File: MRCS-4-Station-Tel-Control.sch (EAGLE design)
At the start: 19 parts, among them CON1 LEDs and Buttons RJ, CON2 LEDS & Pwr RJ, J1 LEDs & Buttons ST, J2 LEDS & Pwr ST

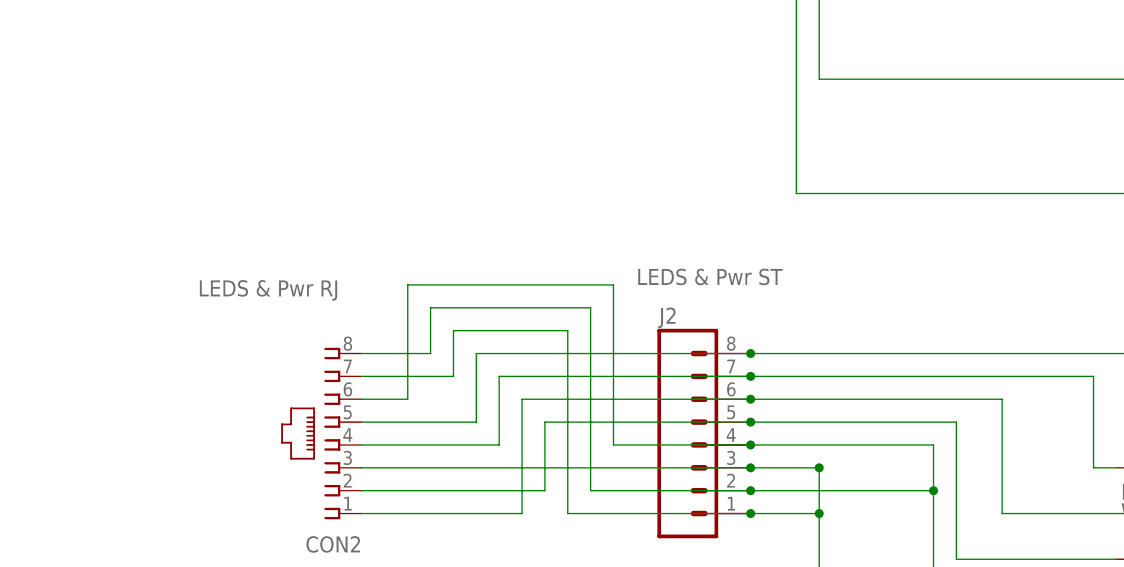
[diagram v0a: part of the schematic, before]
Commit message: Moved labels for push buttons and LEDs to back
A learning exercise involving mirror, rotate and a lot of moving traces from top to bottom and vice versa
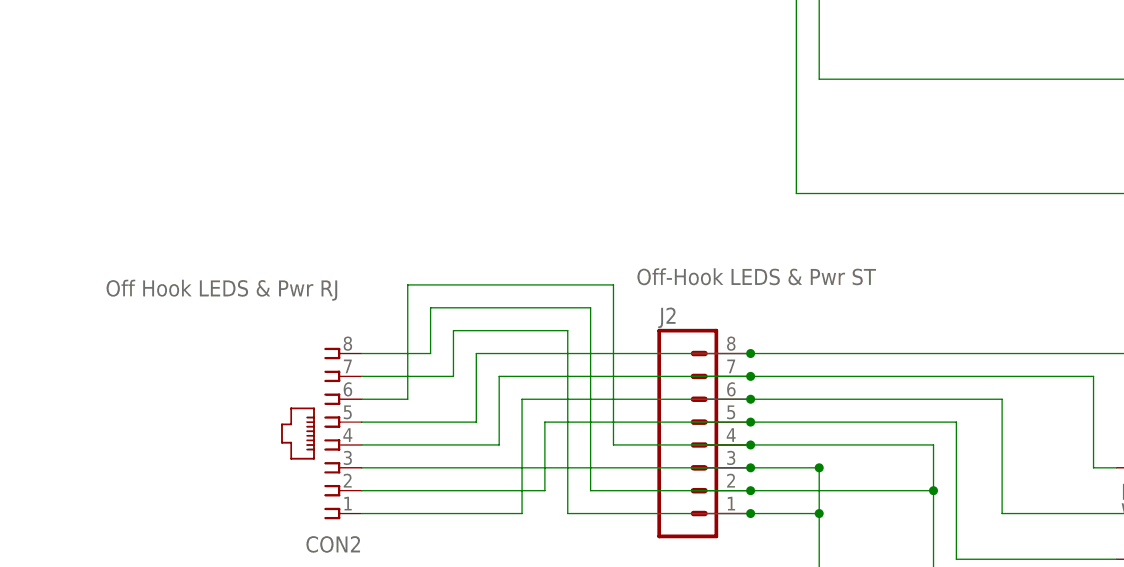
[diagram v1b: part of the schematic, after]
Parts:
- CON2: value LEDS & Pwr RJ -> Off Hook LEDS & Pwr RJ
- J2: value LEDS & Pwr ST -> Off-Hook LEDS & Pwr ST
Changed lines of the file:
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@@
 <part name="LED8" library="SPCoast" deviceset="LED*" device="LED5MM" value="White"/>
 <part name="J1" library="SPCoast" deviceset="CONNECTOR-M08" device="LOCK" value="LEDs &amp; Buttons ST"/>
-<part name="J2" library="SPCoast" deviceset="CONNECTOR-M08" device="LOCK" value="LEDS &amp; Pwr ST"/>
+<part name="J2" library="SPCoast" deviceset="CONNECTOR-M08" device="LOCK" value="Off-Hook LEDS &amp; Pwr ST"/>
 <part name="CON1" library="SPCoast" deviceset="CONNECTOR-RJ45" device="-FRONT" value="LEDs and Buttons RJ"/>
-<part name="CON2" library="SPCoast" deviceset="CONNECTOR-RJ45" device="-FRONT" value="LEDS &amp; Pwr RJ"/>
+<part name="CON2" library="SPCoast" deviceset="CONNECTOR-RJ45" device="-FRONT" value="Off Hook LEDS &amp; Pwr RJ"/>
 <part name="S1" library="SparkFun-Electromechanical" deviceset="SWITCH-MOMENTARY-2" device="12MM"/>
 <part name="S2" library="SparkFun-Electromechanical" deviceset="SWITCH-MOMENTARY-2" device="12MM"/>
